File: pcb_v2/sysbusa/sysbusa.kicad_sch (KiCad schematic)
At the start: 84 parts, among them J1 bus ula 2, J10 bus rf16 3, J11 bus clu 2, J12 bus clu 3, J19 9V 1A, J2 bus ula 1, J20 VOLTMETER, J21 AMPMETER, J22 bus ioc 2, J23 bus ioc 1, J24 bus ioc 3, J26 bus clock, J3 bus rf16 1, J4 bus rf16 2, J5 bus mem 1, J6 bus mem 2, J7 bus clu 1, J8 bus mgrf 1, J9 bus mgrf 2, Q1 BC548, Q2 BC548, U1 MC14495P, U10 MC14495P, U11 IR_HIGH, U13 MC14495P, U14 RDADDR_LOW, U17 RDADDR_HIGH, U2 IR_HIGH, U21 MC14495P, U22 WRADDR_HIGH, U23 WRADDR_LOW, U3 MC14495P, U31 MC14495P, U34 LM7805, U4 IR_LOW, U5 74LS08, U9 IR_LOW

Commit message: movendo itens da clu para o sysbus
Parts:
- added C3, C4, C5: 100nF, Capacitor_THT:C_Disc_D5.1mm_W3.2mm_P5.00mm, symbol Device:C
- added C6: 4.7uF, Capacitor_THT:CP_Radial_D5.0mm_P2.50mm, symbol Device:C_Polarized
- added D1: PWR, LED_THT:LED_D5.0mm, symbol Device:LED
- added R23: 1K, Resistor_THT:R_Axial_DIN0207_L6.3mm_D2.5mm_P7.62mm_Horizontal, symbol Device:R
- added R24: 10K, Resistor_THT:R_Axial_DIN0207_L6.3mm_D2.5mm_P7.62mm_Horizontal, symbol Device:R
- added SW1: RESET, Button_Switch_THT:SW_PUSH_6mm, symbol Switch:SW_Push
- added U12: DATA N0, 7segdisplay:1-digit-13mm, symbol Display_Character:SA39-11EWA
- added unit 4 of U5
- added unit 5 of U5
- added unit 3 of U5
- added unit 2 of U5
- added U6, U8: MC14495P, Package_DIP:DIP-16_W7.62mm, symbol Driver_LED:MC14495P
- added U7: DATA N1, 7segdisplay:1-digit-13mm, symbol Display_Character:SA39-11EWA
- J19, J20, J21: footprint (none) -> Connector_Molex:Molex_KK-254_AE-6410-02A_1x02_P2.54mm_Vertical
- R1, R10, R11, R12, R13, R14, R15, R16, R17, R18, R19, R2, R20, R3, R36, R37, R38, R39, R4, R40, R41, R42, R43, R44, R45, R46, R47, R48, R49, R5, R50, R51, R6, R7, R8, R9: footprint (none) -> Resistor_THT:R_Axial_DIN0207_L6.3mm_D2.5mm_P7.62mm_Horizontal
- U11: value IR_HIGH -> ADDR N1
- U2: value IR_HIGH -> ADDR N3
- U4: value IR_LOW -> ADDR N2
- U5: footprint (none) -> Package_DIP:DIP-14_W7.62mm
- U9: value IR_LOW -> ADDR N0
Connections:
- net INS_{0} is gone; now on net ADDR_{8}: U3.5 (A)
- net INS_{1} is gone; now on net ADDR_{9}: U3.6 (B)
- net INS_{2} is gone; now on net ADDR_{10}: U3.9 (C)
- net INS_{3} is gone; now on net ADDR_{11}: U3.10 (D)
- net +5V: now also C3.2, C4.2, C5.2, C6.1, R23.1, SW1.1, U5.14 (VCC), U6.16 (VCC), U8.16 (VCC)
- net ADDR_{0}: now also U31.5 (A)
- net ADDR_{12}: now also U1.5 (A)
- net ADDR_{13}: now also U1.6 (B)
- net ADDR_{14}: now also U1.9 (C)
- net ADDR_{15}: now also U1.10 (D)
- net ADDR_{1}: now also U31.6 (B)
- net ADDR_{2}: now also U31.9 (C)
- net ADDR_{3}: now also U31.10 (D)
- net ADDR_{4}: now also U10.5 (A)
- net ADDR_{5}: now also U10.6 (B)
- net ADDR_{6}: now also U10.9 (C)
- net ADDR_{7}: now also U10.10 (D)
- net DATA_{0}: now also U8.5 (A)
- net DATA_{1}: now also U8.6 (B)
- net DATA_{2}: now also U8.9 (C)
- net DATA_{3}: now also U8.10 (D)
- net DATA_{4}: now also U6.5 (A)
- net DATA_{5}: now also U6.6 (B)
- net DATA_{6}: now also U6.9 (C)
- net DATA_{7}: now also U6.10 (D)
- net GND: now also C3.1, C4.1, C5.1, D1.1 (K), R24.2, U12.3 (CA), U12.8 (CA), U5.7 (GND), U6.7 (~{CLK}), U6.8 (GND), U7.3 (CA), U7.8 (CA), U8.7 (~{CLK}), U8.8 (GND)
- net RESET: now reaches J12.9 (Pin_9)
- net RESET: now also J26.10 (Pin_10), U5.8
- removed net INS_{4}: U1.5 (A), U10.5 (A)
- removed net INS_{5}: U1.6 (B), U10.6 (B)
- removed net INS_{6}: U1.9 (C), U10.9 (C)
- removed net INS_{7}: U1.10 (D), U10.10 (D)
- new net: D1.2 (A), R23.2
- new net: U12.4 (E), U8.1 (e)
- new net: U12.10 (A), U8.12 (a)
- new net: U12.9 (B), U8.13 (b)
- new net: U12.7 (C), U8.14 (c)
- new net: U12.5 (D), U8.15 (d)
- new net: U12.2 (F), U8.2 (f)
- new net: U12.1 (G), U8.3 (g)
- new net: C6.2, R24.1, SW1.2, U5.10, U5.9
- new net: U6.3 (g), U7.1 (G)
- new net: U6.12 (a), U7.10 (A)
- new net: U6.2 (f), U7.2 (F)
- new net: U6.1 (e), U7.4 (E)
- new net: U6.15 (d), U7.5 (D)
- new net: U6.14 (c), U7.7 (C)
- new net: U6.13 (b), U7.9 (B)
- no-connect marks 83 -> 93
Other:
- moved on the sheet: C1, C10, C13, C2, C21, C31, Q1, Q2, R1, R10, R11, R12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

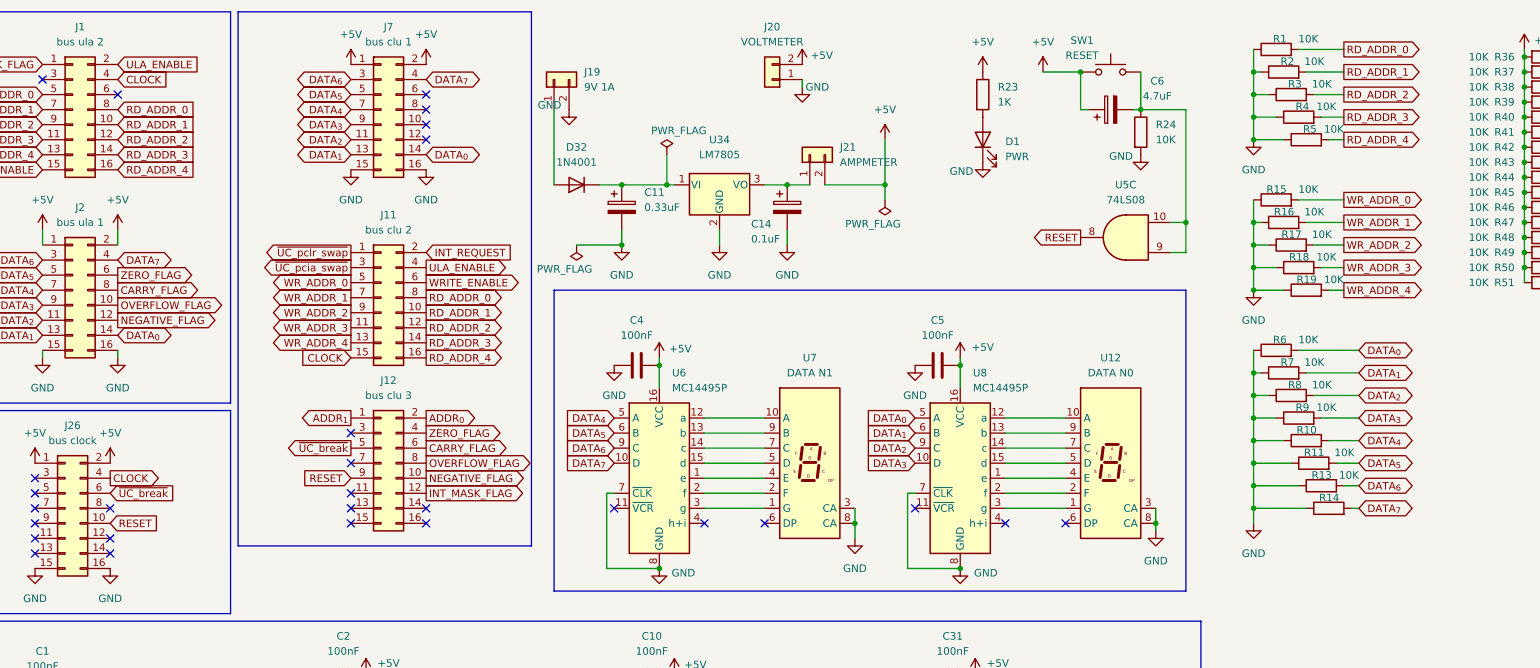
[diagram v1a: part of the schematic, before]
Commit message: placa clock gerando os sinais clock e n_clock sincronizados
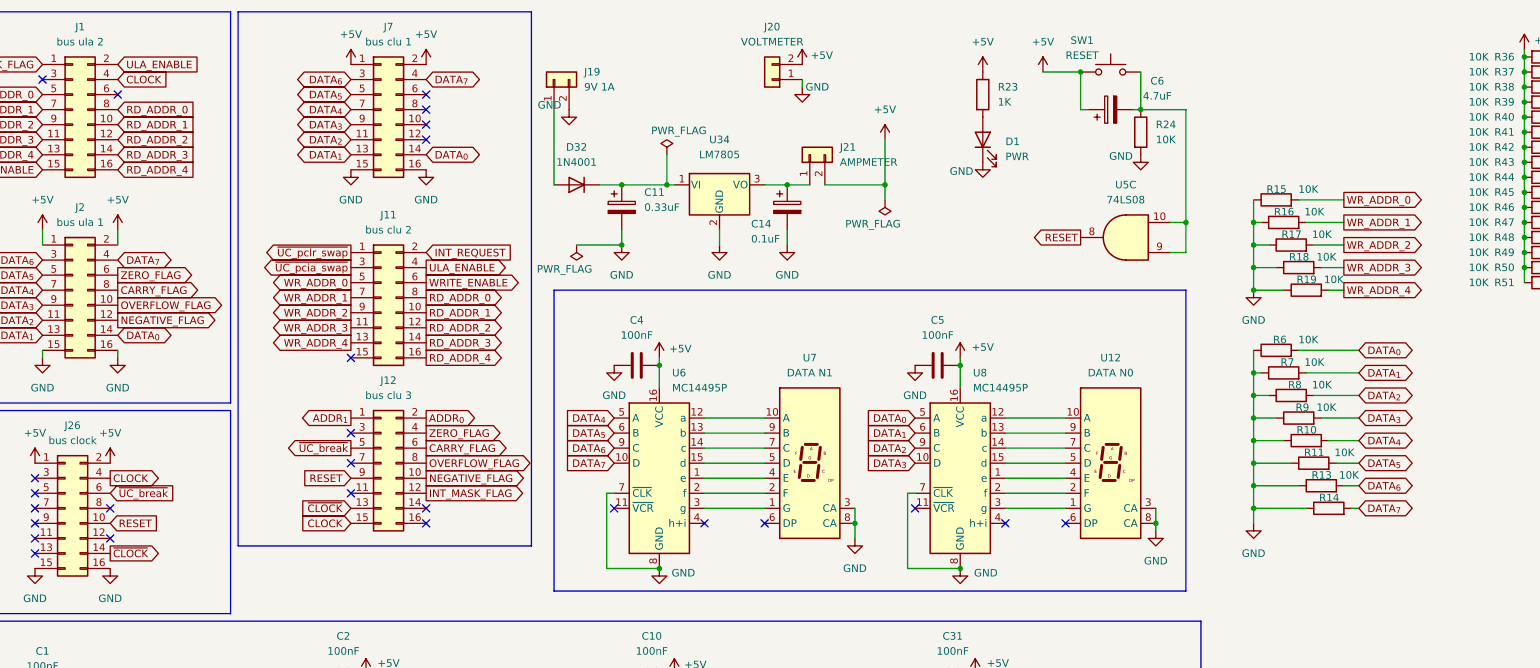
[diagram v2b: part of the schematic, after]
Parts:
- removed R1, R2, R3, R4, R5: 10K, Resistor_THT:R_Axial_DIN0207_L6.3mm_D2.5mm_P7.62mm_Horizontal, symbol Device:R
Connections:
- net CLOCK: now also J12.15 (Pin_15); no longer J11.15 (Pin_15)
- net ~{CLOCK}: now reaches J12.13 (Pin_13)
- net ~{CLOCK}: now also J26.14 (Pin_14)
- no-connect marks 93 -> 91

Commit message: padronização de conector de IO; ideias para o layout do backplane
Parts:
- renumbered C6 to C2, C2 to C3, C3 to C5, C4 to C6, C5 to C8
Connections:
- net +5V: now also U5.12, U5.13, U5.4, U5.5
- net WR_ADDR_0: now also J24.5 (Pin_5); no longer J24.1 (Pin_1)
- net WR_ADDR_1: now also J24.7 (Pin_7); no longer J24.3 (Pin_3)
- net WR_ADDR_2: now also J24.9 (Pin_9); no longer J24.5 (Pin_5)
- net WR_ADDR_3: now also J24.11 (Pin_11); no longer J24.7 (Pin_7)
- net WR_ADDR_4: now also J24.13 (Pin_13); no longer J24.9 (Pin_9)
- no-connect marks 91 -> 87
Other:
- moved on the sheet: U5A, U5B, U5D

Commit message: definindo o layout para empilhar as placas
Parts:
- added R1: 470R, Resistor_THT:R_Axial_DIN0207_L6.3mm_D2.5mm_P7.62mm_Horizontal, symbol Device:R
- SW1: footprint Button_Switch_THT:SW_PUSH_6mm -> Connector_Molex:Molex_KK-254_AE-6410-02A_1x02_P2.54mm_Vertical
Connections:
- net GND: now also R1.2; no longer Q1.1 (C)
- new net: Q1.1 (C), R1.1
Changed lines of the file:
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@@
 	(wire
 		(pts
+			(xy 139.7 256.54) (xy 140.97 256.54)
+		)
+		(stroke
+			(width 0)
+			(type default)
+		)
+	)
+	(wire
+		(pts
 			(xy 336.55 55.88) (xy 336.55 59.69)
 		)
@@
 	(symbol
 		(lib_id "Device:R")
+		(at 144.78 256.54 270)
+		(unit 1)
+		(exclude_from_sim no)
+		(in_bom yes)
+		(on_board yes)
+		(dnp no)
+		(property "Reference" "R1"
+			(at 151.13 257.302 90)
+			(effects
+				(font
+					(size 1.27 1.27)
+				)
+			)
+		)
+		(property "Value" "470R"
+			(at 149.606 259.334 90)
+			(effects
+				(font
+					(size 1.27 1.27)
+				)
+			)
+		)
+		(property "Footprint" "Resistor_THT:R_Axial_DIN0207_L6.3mm_D2.5mm_P7.62mm_Horizontal"
+			(at 144.78 254.762 90)
+			(effects
+				(font
+					(size 1.27 1.27)
+				)
+				(hide yes)
+			)
+		)
+		(property "Datasheet" "~"
+			(at 144.78 256.54 0)
+			(effects
+				(font
+					(size 1.27 1.27)
+				)
+				(hide yes)
+			)
+		)
+		(property "Description" "Resistor"
+			(at 144.78 256.54 0)
+			(effects
+				(font
+					(size 1.27 1.27)
+				)
+				(hide yes)
+			)
+		)
+		(pin "1"
+		)
+		(pin "2"
+		)
+		(instances
+			(project "sysbusa"
+				(path "/02b9996c-8125-4412-af70-f1d12218c07b"
+					(reference "R1")
+					(unit 1)
+				)
+			)
+		)
+	)
+	(symbol
+		(lib_id "Device:R")
 		(at 340.36 69.85 90)
 		(unit 1)
@@
 			)
 		)
-		(property "Footprint" "Button_Switch_THT:SW_PUSH_6mm"
+		(property "Footprint" "Connector_Molex:Molex_KK-254_AE-6410-02A_1x02_P2.54mm_Vertical"
 			(at 312.42 17.78 0)
 			(effects
@@
 		(on_board yes)
 		(dnp no)
-		(fields_autoplaced yes)
 		(property "Reference" "R21"
-			(at 137.16 257.81 90)
+			(at 131.318 255.016 90)
 			(effects
 				(font
@@
 		)
 		(property "Value" "10K"
-			(at 137.16 255.27 90)
+			(at 131.064 257.048 90)
 			(effects
 				(font
@@
 	(symbol
 		(lib_id "power:GND")
-		(at 148.59 256.54 0)
+		(at 139.7 256.54 0)
 		(unit 1)
 		(exclude_from_sim no)
@@
 		(dnp no)
 		(property "Reference" "#PWR081"
-			(at 148.59 262.89 0)
+			(at 139.7 262.89 0)
 			(effects
 				(font
@@
 		)
 		(property "Value" "GND"
-			(at 145.034 257.81 0)
+			(at 136.144 257.81 0)
 			(effects
 				(font
@@
 		)
 		(property "Footprint" ""
-			(at 148.59 256.54 0)
+			(at 139.7 256.54 0)
 			(effects
 				(font
@@
 		)
 		(property "Datasheet" ""
-			(at 148.59 256.54 0)
+			(at 139.7 256.54 0)
 			(effects
 				(font
@@
 		)
 		(property "Description" "Power symbol creates a global label with name \"GND\" , ground"
-			(at 148.59 256.54 0)
+			(at 139.7 256.54 0)
 			(effects
 				(font

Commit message: refazendo os pcbs para caber em folha A4
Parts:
- removed J8: bus mgrf 1, Connector_PinHeader_2.54mm:PinHeader_2x08_P2.54mm_Vertical, symbol Connector_Generic:Conn_02x08_Odd_Even
- removed J9: bus mgrf 2, Connector_PinHeader_2.54mm:PinHeader_2x08_P2.54mm_Vertical, symbol Connector_Generic:Conn_02x08_Odd_Even
- added R2, R25, R3, R4, R5: 10K, Resistor_THT:R_Axial_DIN0207_L6.3mm_D2.5mm_P7.62mm_Horizontal, symbol Device:R
- U11, U12, U14, U17, U2, U22, U23, U4, U7, U9: footprint 7segdisplay:1-digit-13mm -> Display_7Segment:Sx39-1xxxxx
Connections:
- net GND: now also R2.1, R25.1, R3.1, R4.1, R5.1
- net RD_ADDR_0: now also R2.2
- net RD_ADDR_1: now also R5.2
- net RD_ADDR_2: now also R25.2
- net RD_ADDR_3: now also R4.2
- net RD_ADDR_4: now also R3.2
- net at U22.3 (CA), U22.8 (CA): now also Q2.1 (C); no longer Q2.3 (E)
- net at R20.1: now also Q2.3 (E); no longer Q2.1 (C)
- net at Q1.1 (C): now also U23.3 (CA), U23.8 (CA); no longer R1.1
- new net: Q1.3 (E), R1.1
- no-connect marks 87 -> 78

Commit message: posicionamento dos conectores com os demais módulos
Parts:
- J19, J20, J21, SW1: footprint Connector_Molex:Molex_KK-254_AE-6410-02A_1x02_P2.54mm_Vertical -> Connector_JST:JST_XH_B2B-XH-A_1x02_P2.50mm_Vertical
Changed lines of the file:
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@@
 			)
 		)
-		(property "Footprint" "Connector_Molex:Molex_KK-254_AE-6410-02A_1x02_P2.54mm_Vertical"
+		(property "Footprint" "Connector_JST:JST_XH_B2B-XH-A_1x02_P2.50mm_Vertical"
 			(at 255.27 24.13 0)
 			(effects
@@
 			)
 		)
-		(property "Footprint" "Connector_Molex:Molex_KK-254_AE-6410-02A_1x02_P2.54mm_Vertical"
+		(property "Footprint" "Connector_JST:JST_XH_B2B-XH-A_1x02_P2.50mm_Vertical"
 			(at 218.44 24.13 0)
 			(effects
@@
 			)
 		)
-		(property "Footprint" "Connector_Molex:Molex_KK-254_AE-6410-02A_1x02_P2.54mm_Vertical"
+		(property "Footprint" "Connector_JST:JST_XH_B2B-XH-A_1x02_P2.50mm_Vertical"
 			(at 312.42 17.78 0)
 			(effects
@@
 		)
 		(instances
-			(project ""
+			(project "sysbusa"
 				(path "/02b9996c-8125-4412-af70-f1d12218c07b"
 					(reference "C2")
@@
 			)
 		)
-		(property "Footprint" "Connector_Molex:Molex_KK-254_AE-6410-02A_1x02_P2.54mm_Vertical"
+		(property "Footprint" "Connector_JST:JST_XH_B2B-XH-A_1x02_P2.50mm_Vertical"
 			(at 261.62 36.83 0)
 			(effects

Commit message: inicio do layout da pcb
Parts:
- removed C5: 100nF, Capacitor_THT:C_Disc_D5.1mm_W3.2mm_P5.00mm, symbol Device:C
- removed R10, R11, R13, R14, R15, R16, R17, R18, R19, R2, R25, R3, R36, R37, R38, R39, R4, R40, R41, R42, R43, R44, R45, R46, R47, R48, R49, R5, R50, R51, R6, R7, R8, R9: 10K, Resistor_THT:R_Axial_DIN0207_L6.3mm_D2.5mm_P7.62mm_Horizontal, symbol Device:R
- removed U5: 74LS08, Package_DIP:DIP-14_W7.62mm, symbol 74xx:74LS08
- added RN1, RN2, RN3: 10K, Resistor_THT:R_Array_SIP9, symbol Device:R_Network08
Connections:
- net ADDR_{0}: now also RN3.2 (R1)
- net ADDR_{10}: now also RN2.4 (R3)
- net ADDR_{11}: now also RN2.5 (R4)
- net ADDR_{12}: now also RN2.6 (R5)
- net ADDR_{13}: now also RN2.7 (R6)
- net ADDR_{14}: now also RN2.8 (R7)
- net ADDR_{15}: now also RN2.9 (R8)
- net ADDR_{1}: now also RN3.3 (R2)
- net ADDR_{2}: now also RN3.4 (R3)
- net ADDR_{3}: now also RN3.5 (R4)
- net ADDR_{4}: now also RN3.6 (R5)
- net ADDR_{5}: now also RN3.7 (R6)
- net ADDR_{6}: now also RN3.8 (R7)
- net ADDR_{7}: now also RN3.9 (R8)
- net ADDR_{8}: now also RN2.2 (R1)
- net ADDR_{9}: now also RN2.3 (R2)
- net DATA_{0}: now also RN1.9 (R8)
- net DATA_{1}: now also RN1.8 (R7)
- net DATA_{2}: now also RN1.7 (R6)
- net DATA_{3}: now also RN1.6 (R5)
- net DATA_{4}: now also RN1.5 (R4)
- net DATA_{5}: now also RN1.4 (R3)
- net DATA_{6}: now also RN1.3 (R2)
- net DATA_{7}: now also RN1.2 (R1)
- net GND: now also RN1.1 (common), RN2.1 (common), RN3.1 (common)
- net RESET: now also C2.2, R24.1, SW1.2
- no-connect marks 78 -> 76
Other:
- note added: "MELHORAR O CIRCUITO DE RESET"
